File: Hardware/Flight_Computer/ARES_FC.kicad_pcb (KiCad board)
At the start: 2 copper layers, 57.2 x 57.2 mm, 67 parts, among them J1 SWD, J2 TYPE-C-31-M-12, J3 FC_M/P, J4 5V, J5 GND, J6 FC_RF, J7 Conn_01x04_Pin, J8 Conn_01x04_Pin, U1 STM32F401CCU6, U2 AMS1117-3.3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

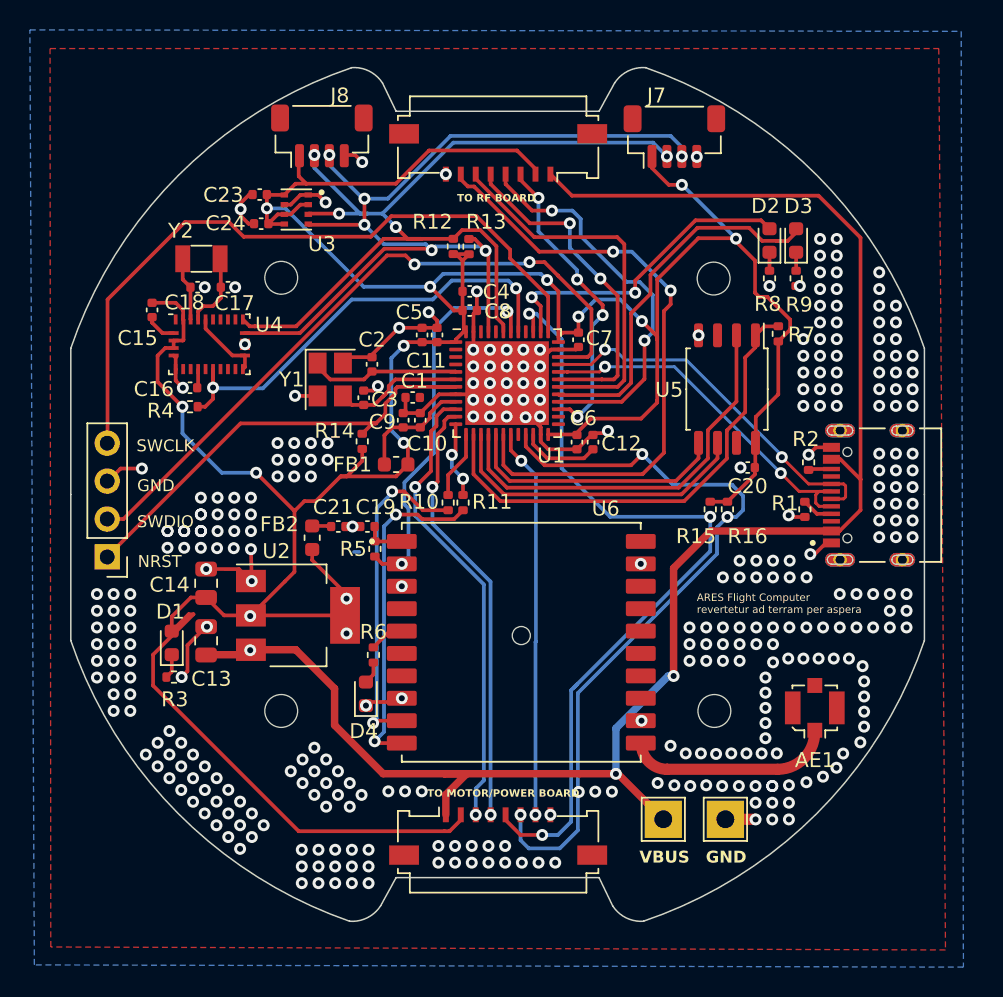
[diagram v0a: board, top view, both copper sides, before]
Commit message: changed C4 to 0603; removed vias on pads; added stitching vias
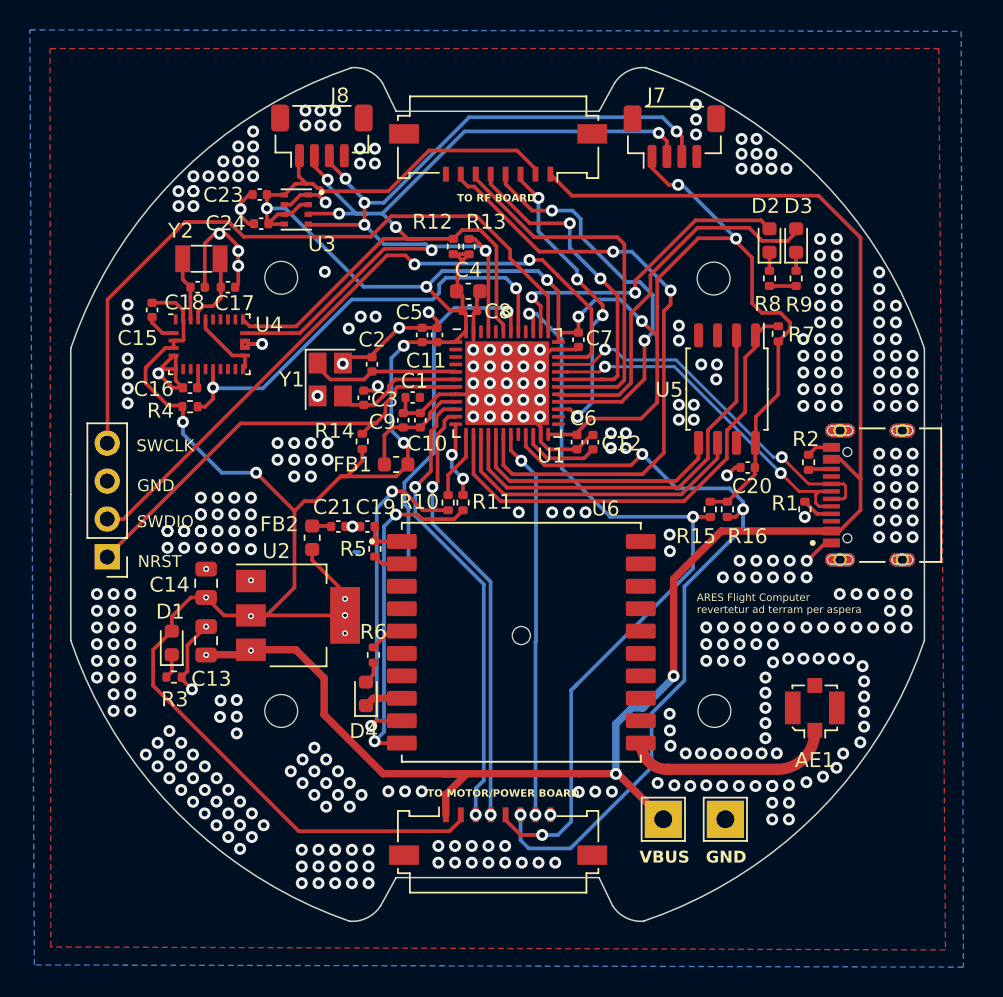
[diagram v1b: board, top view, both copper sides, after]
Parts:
- C4: footprint Capacitor_SMD:C_0402_1005Metric -> Capacitor_SMD:C_0603_1608Metric
- FB2: value 120R -> 600R
- moved C4 0.10 mm to (148.0, 85.9)
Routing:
- net GND: track 81.0 -> 86.2 mm, vias 343 -> 398
- net /MOTOR_SCL: track 51.0 -> 52.0 mm
- net /SCL: track 64.8 -> 65.4 mm
- net /SDA: track 62.0 -> 62.6 mm
- net +3.3V: track 235.3 -> 234.9 mm, vias 14 -> 17
- net VBUS: track 115.3 -> 115.1 mm, vias 3 -> 4
- net /GPS_NRST: vias 2 -> 1

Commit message: fixed JLC part numbers and ran DRC
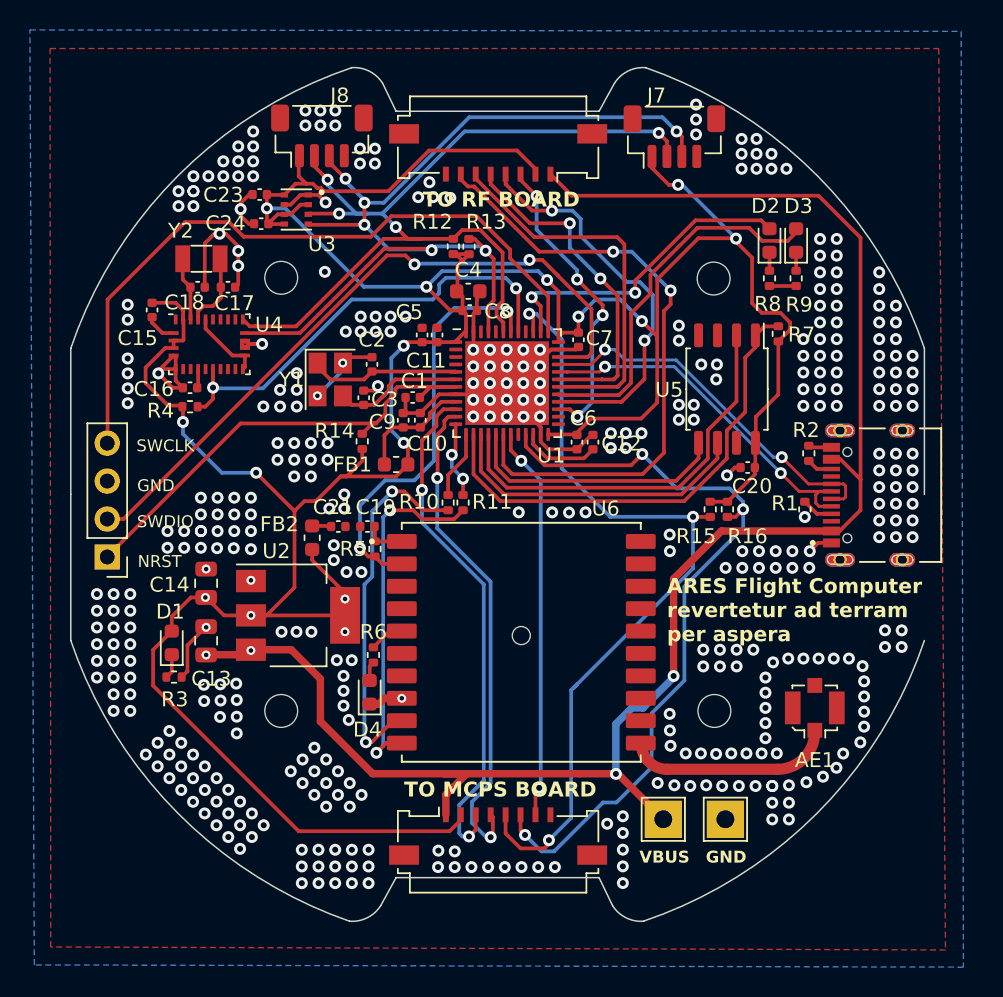
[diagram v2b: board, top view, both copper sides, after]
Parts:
- moved R2 0.60 mm to (170.8, 96.8)
- moved D4 0.27 mm to (141.4, 112.8)
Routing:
- net GND: track 86.2 -> 78.5 mm, vias 398 -> 406
- net /S2_MP: track 29.2 -> 33.3 mm
- net /S1_MP: track 30.9 -> 34.6 mm
- net Net-(U6-TX): track 22.7 -> 24.9 mm
- net /GPS_NRST: track 26.3 -> 28.2 mm, vias 1 -> 2
- net Net-(U6-RX): track 22.5 -> 24.0 mm
- net /MOTOR_SDA: track 53.8 -> 55.1 mm
- net /NRST: track 31.5 -> 32.7 mm
- net /SCL: track 65.4 -> 65.9 mm
- net +3.3V: vias 17 -> 15
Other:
- board text added: "TO MCPS BOARD"
- board text removed: "TO MOTOR/POWER BOARD"

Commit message: some DRC warnings fixed
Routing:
- net GND: vias 406 -> 403
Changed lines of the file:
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@@
+		(layer "Edge.Cuts")
+	)
+	(gr_line
+		(start 178.538742 109.2818)
+		(end 178.538742 99.5028)
+		(stroke
+			(width 0.1)
+			(type solid)
+		)
 		(layer "Edge.Cuts")
 	)
@@
 	)
 	(via
+		(at 136.517599 91.3824)
+		(size 0.8)
+		(drill 0.4)
+		(layers "F.Cu" "B.Cu")
+		(free yes)
+		(net 2)
+	)
+	(via
+		(at 167.3 75.7)
+		(size 0.8)
+		(drill 0.4)
+		(layers "F.Cu" "B.Cu")
+		(net 2)
+	)
+	(via
+		(at 124.2568 110.6424)
+		(size 0.8)
+		(drill 0.4)
+		(layers "F.Cu" "B.Cu")
+		(free yes)
+		(net 2)
+	)
+	(via
+		(at 177.7492 102.362)
+		(size 0.8)
+		(drill 0.4)
+		(layers "F.Cu" "B.Cu")
+		(free yes)
+		(net 2)
+	)
+	(via
+		(at 148.336 93.167201)
+		(size 0.8)
+		(drill 0.4)
+		(layers "F.Cu" "B.Cu")
+		(free yes)
+		(net 2)
+	)
+	(via
+		(at 158.35 124.4028)
+		(size 0.8)
+		(drill 0.4)
+		(layers "F.Cu" "B.Cu")
+		(free yes)
+		(net 2)
+	)
+	(via
+		(at 138.486526 120.407451)
+		(size 0.8)
+		(drill 0.4)
+		(layers "F.Cu" "B.Cu")
+		(free yes)
+		(net 2)
+	)
+	(via
+		(at 132.334 99.7204)
+		(size 0.8)
+		(drill 0.4)
+		(layers "F.Cu" "B.Cu")
+		(free yes)
+		(net 2)
+	)
+	(via
+		(at 176.6316 101.2444)
+		(size 0.8)
+		(drill 0.4)
+		(layers "F.Cu" "B.Cu")
+		(free yes)
+		(net 2)
+	)
+	(via
+		(at 162.56 116.84)
+		(size 0.8)
+		(drill 0.4)
+		(layers "F.Cu" "B.Cu")
+		(free yes)
+		(net 2)
+	)
+	(via
+		(at 161.798 118.9736)
+		(size 0.8)
+		(drill 0.4)
+		(layers "F.Cu" "B.Cu")
+		(free yes)
+		(net 2)
+	)
+	(via
+		(at 126.412937 116.919063)
+		(size 0.8)
+		(drill 0.4)
+		(layers "F.Cu" "B.Cu")
+		(free yes)
+		(net 2)
+	)
+	(via
+		(at 152.8064 92.0496)
+		(size 0.8)
+		(drill 0.4)
+		(layers "F.Cu" "B.Cu")
+		(free yes)
+		(net 2)
+	)
+	(via
+		(at 167.898 111.76)
+		(size 0.8)
+		(drill 0.4)
+		(layers "F.Cu" "B.Cu")
+		(free yes)
+		(net 2)
+	)
+	(via
+		(at 129.573988 116.919063)
+		(size 0.8)
+		(drill 0.4)
+		(layers "F.Cu" "B.Cu")
+		(free yes)
+		(net 2)
+	)
+	(via
+		(at 151.6888 93.1672)
+		(size 0.8)
+		(drill 0.4)
+		(layers "F.Cu" "B.Cu")
+		(free yes)
+		(net 2)
+	)
+	(via
 		(at 129.6 79.2)
 		(size 0.8)
@@
 	)
 	(via
-		(at 136.517599 91.3824)
-		(size 0.8)
-		(drill 0.4)
-		(layers "F.Cu" "B.Cu")
-		(free yes)
-		(net 2)
-	)
-	(via
-		(at 167.3 75.7)
-		(size 0.8)
-		(drill 0.4)
-		(layers "F.Cu" "B.Cu")
-		(net 2)
-	)
-	(via
-		(at 124.2568 110.6424)
-		(size 0.8)
-		(drill 0.4)
-		(layers "F.Cu" "B.Cu")
-		(free yes)
-		(net 2)
-	)
-	(via
-		(at 177.7492 102.362)
-		(size 0.8)
-		(drill 0.4)
-		(layers "F.Cu" "B.Cu")
-		(free yes)
-		(net 2)
-	)
-	(via
-		(at 148.336 93.167201)
-		(size 0.8)
-		(drill 0.4)
-		(layers "F.Cu" "B.Cu")
-		(free yes)
-		(net 2)
-	)
-	(via
-		(at 158.35 124.4028)
-		(size 0.8)
-		(drill 0.4)
-		(layers "F.Cu" "B.Cu")
-		(free yes)
-		(net 2)
-	)
-	(via
-		(at 138.486526 120.407451)
-		(size 0.8)
-		(drill 0.4)
-		(layers "F.Cu" "B.Cu")
-		(free yes)
-		(net 2)
-	)
-	(via
-		(at 132.334 99.7204)
-		(size 0.8)
-		(drill 0.4)
-		(layers "F.Cu" "B.Cu")
-		(free yes)
-		(net 2)
-	)
-	(via
-		(at 176.6316 101.2444)
-		(size 0.8)
-		(drill 0.4)
-		(layers "F.Cu" "B.Cu")
-		(free yes)
-		(net 2)
-	)
-	(via
-		(at 162.56 116.84)
-		(size 0.8)
-		(drill 0.4)
-		(layers "F.Cu" "B.Cu")
-		(free yes)
-		(net 2)
-	)
-	(via
-		(at 161.798 118.9736)
-		(size 0.8)
-		(drill 0.4)
-		(layers "F.Cu" "B.Cu")
-		(free yes)
-		(net 2)
-	)
-	(via
-		(at 126.412937 116.919063)
-		(size 0.8)
-		(drill 0.4)
-		(layers "F.Cu" "B.Cu")
-		(free yes)
-		(net 2)
-	)
-	(via
-		(at 168.3512 119.024401)
-		(size 0.8)
-		(drill 0.4)
-		(layers "F.Cu" "B.Cu")
-		(free yes)
-		(net 2)
-	)
-	(via
-		(at 152.8064 92.0496)
-		(size 0.8)
-		(drill 0.4)
-		(layers "F.Cu" "B.Cu")
-		(free yes)
-		(net 2)
-	)
-	(via
-		(at 167.898 111.76)
-		(size 0.8)
-		(drill 0.4)
-		(layers "F.Cu" "B.Cu")
-		(free yes)
-		(net 2)
-	)
-	(via
-		(at 129.573988 116.919063)
-		(size 0.8)
-		(drill 0.4)
-		(layers "F.Cu" "B.Cu")
-		(free yes)
-		(net 2)
-	)
-	(via
-		(at 151.6888 93.1672)
-		(size 0.8)
-		(drill 0.4)
-		(layers "F.Cu" "B.Cu")
-		(free yes)
-		(net 2)
-	)
-	(via
-		(at 129.6 79.2)
-		(size 0.8)
-		(drill 0.4)
-		(layers "F.Cu" "B.Cu")
-		(net 2)
-	)
-	(via
 		(at 132.6 83.2)
 		(size 0.8)
@@
 		(size 0.8)
 		(drill 0.4)
-		(layers "F.Cu" "B.Cu")
-		(free yes)
-		(net 2)
-	)
-	(via
-		(at 130.0988 101.9556)
-		(size 0.8)
-		(drill 0.4)

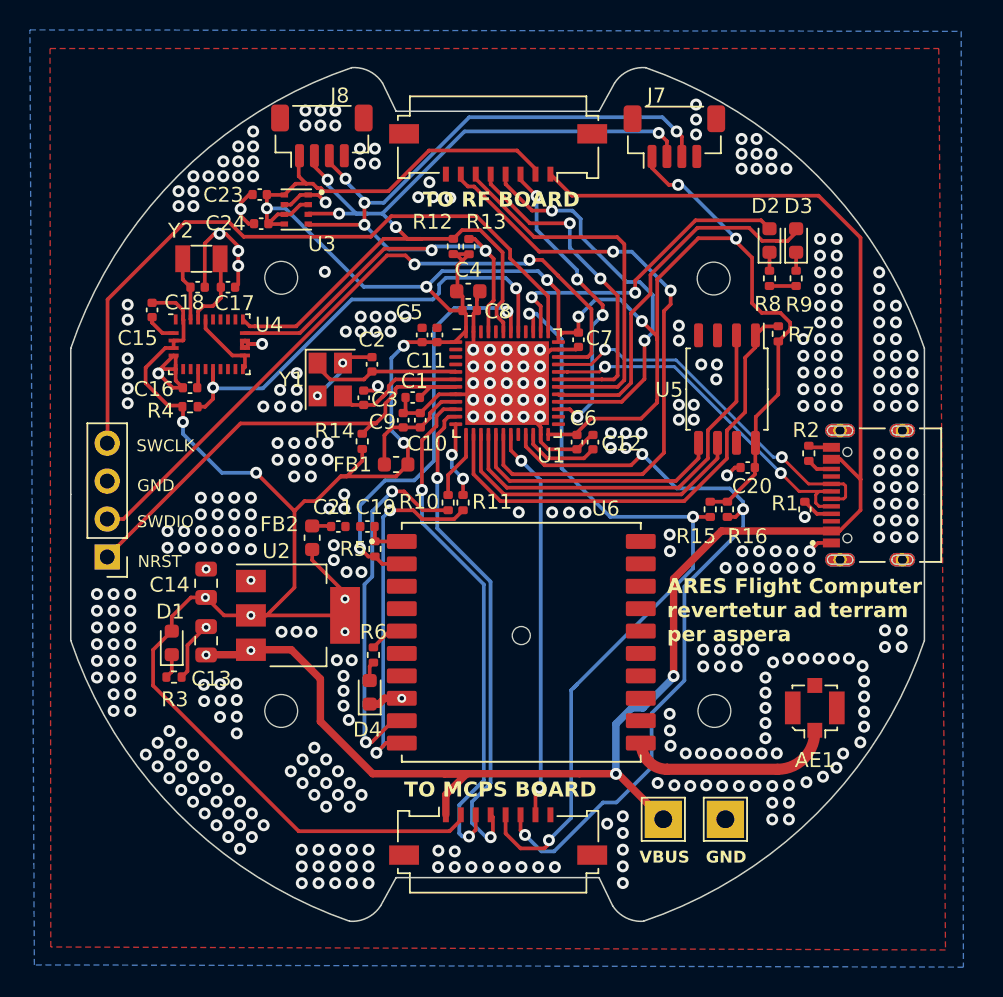
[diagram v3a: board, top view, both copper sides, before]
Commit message: Added more stitching vias to cutoff segments of ground plane Shrunk ViPs from 0.6/0.3 to 0.4/0.2
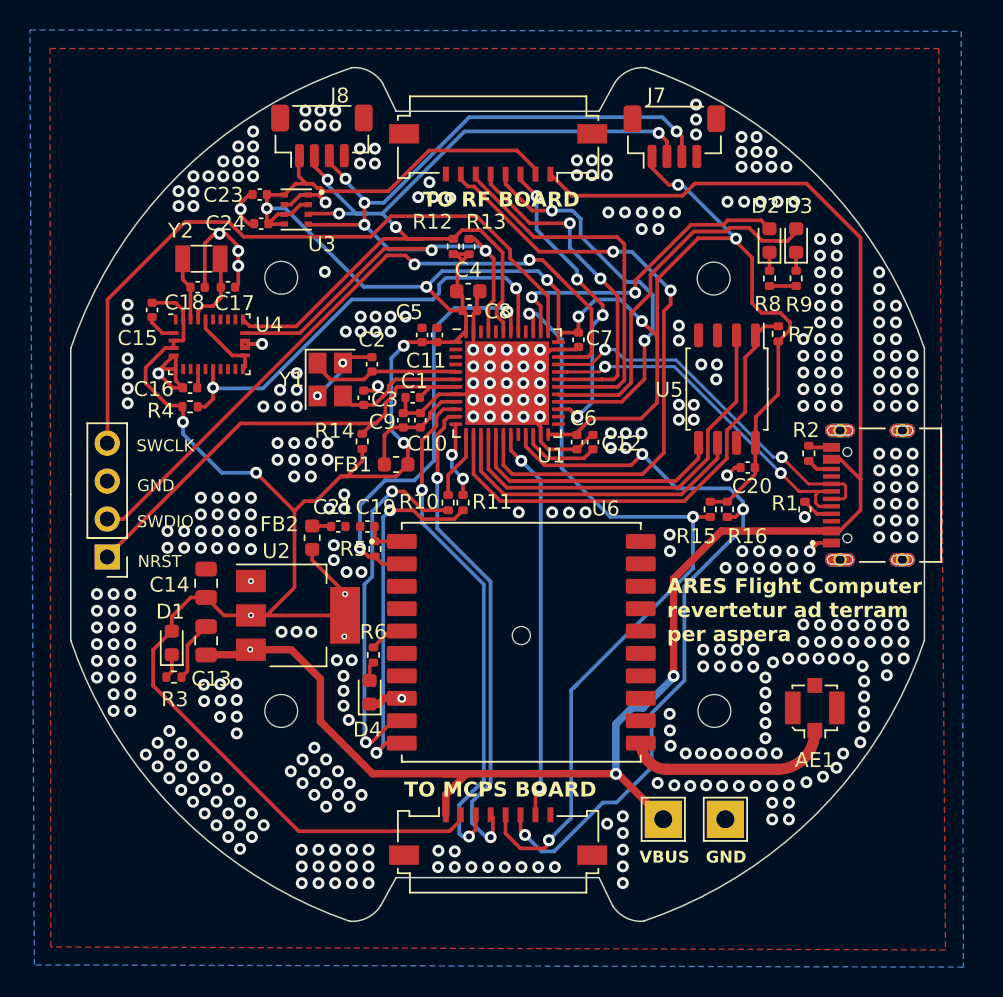
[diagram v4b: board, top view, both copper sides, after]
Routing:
- net VBUS: track 115.4 -> 116.3 mm, vias 4 -> 3
- net GND: track 78.5 -> 78.7 mm, vias 403 -> 433
- net +3.3V: vias 15 -> 14

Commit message: hid silkscreen component labels
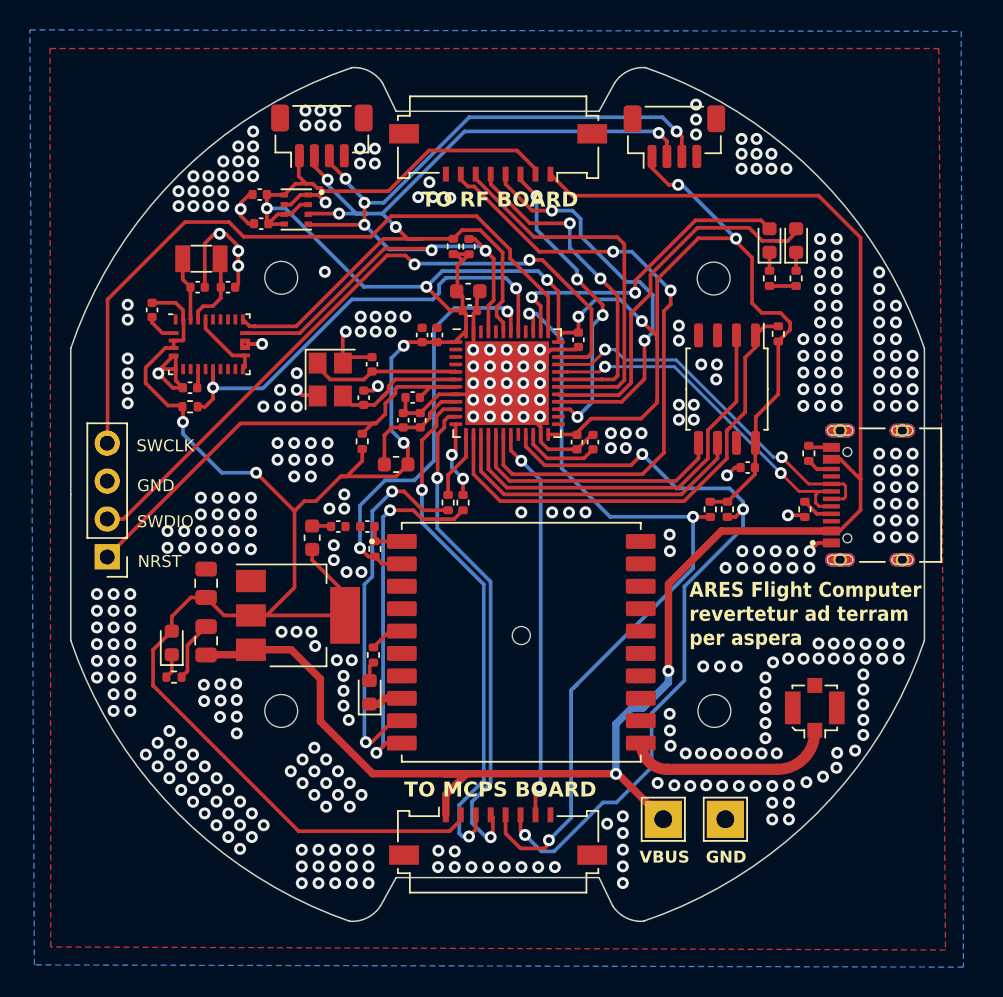
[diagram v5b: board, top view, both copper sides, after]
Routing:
- net GND: track 78.7 -> 81.0 mm, vias 433 -> 403
- net VBUS: track 116.3 -> 115.4 mm, vias 3 -> 2
- net +3.3V: vias 14 -> 11
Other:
- board text removed: "C10"

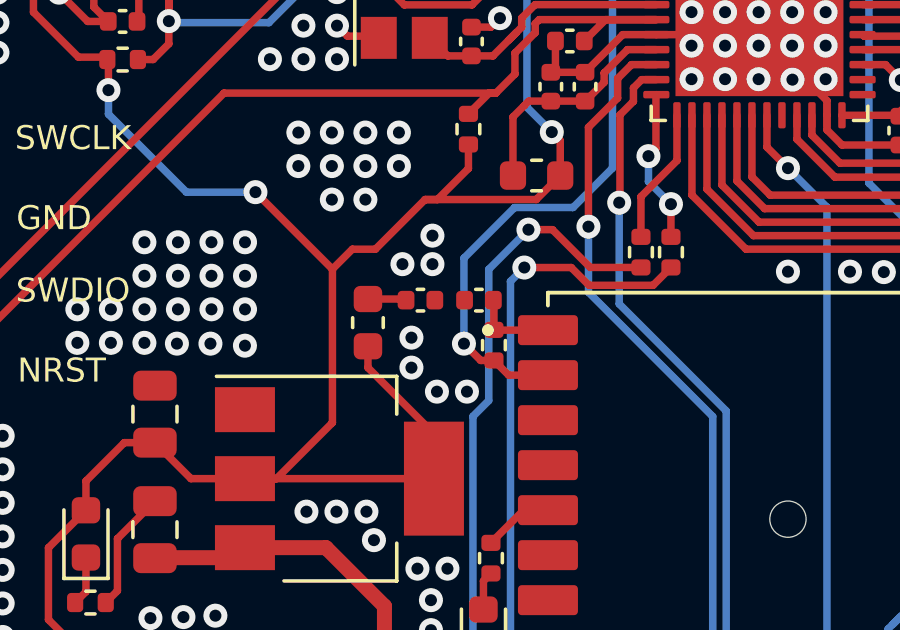
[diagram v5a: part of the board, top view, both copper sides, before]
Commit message: added missing 3.3V bridge connection to GPS PS pin
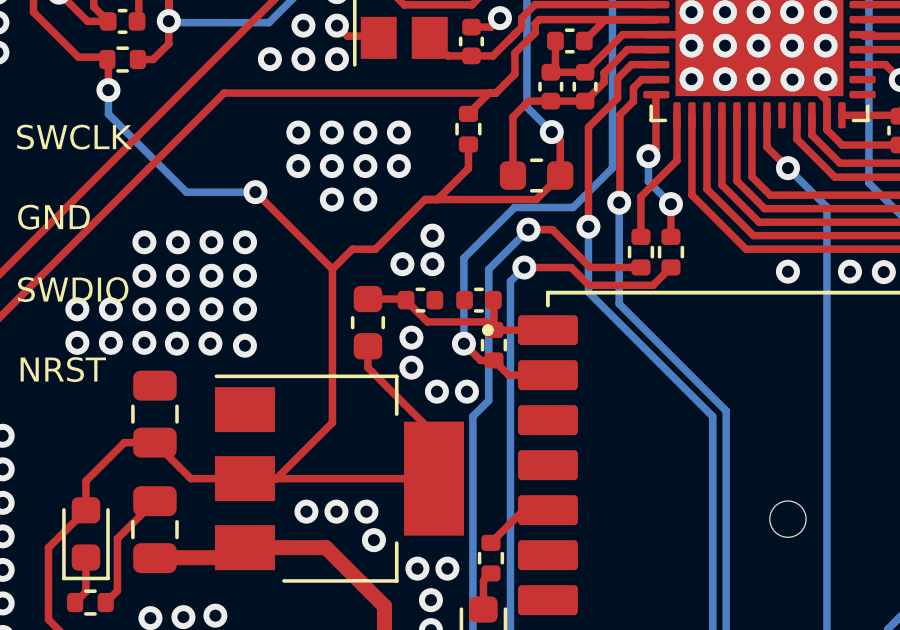
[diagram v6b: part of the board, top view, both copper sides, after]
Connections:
- C21 pad 1: Net-(C21-Pad1) -> Net-(U6-VCC)
- FB2 pad 2: Net-(C21-Pad1) -> Net-(U6-VCC)
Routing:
- net Net-(U6-VCC): track 2.80 -> 7.46 mm
- net Net-(C21-Pad1): track 1.32 -> 0.00 mm
